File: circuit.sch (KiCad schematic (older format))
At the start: 35 parts, among them J1 CONN_8, J2 PASS_LED, J3 FAIL_LED, P1 PASS/FAIL, P2 RESET, Q1 FET-2N7000, Q2 FET-2N7000, Q3 FET-2N7000, U1 OpAmp-TLV2374, U2 Comp-LM339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

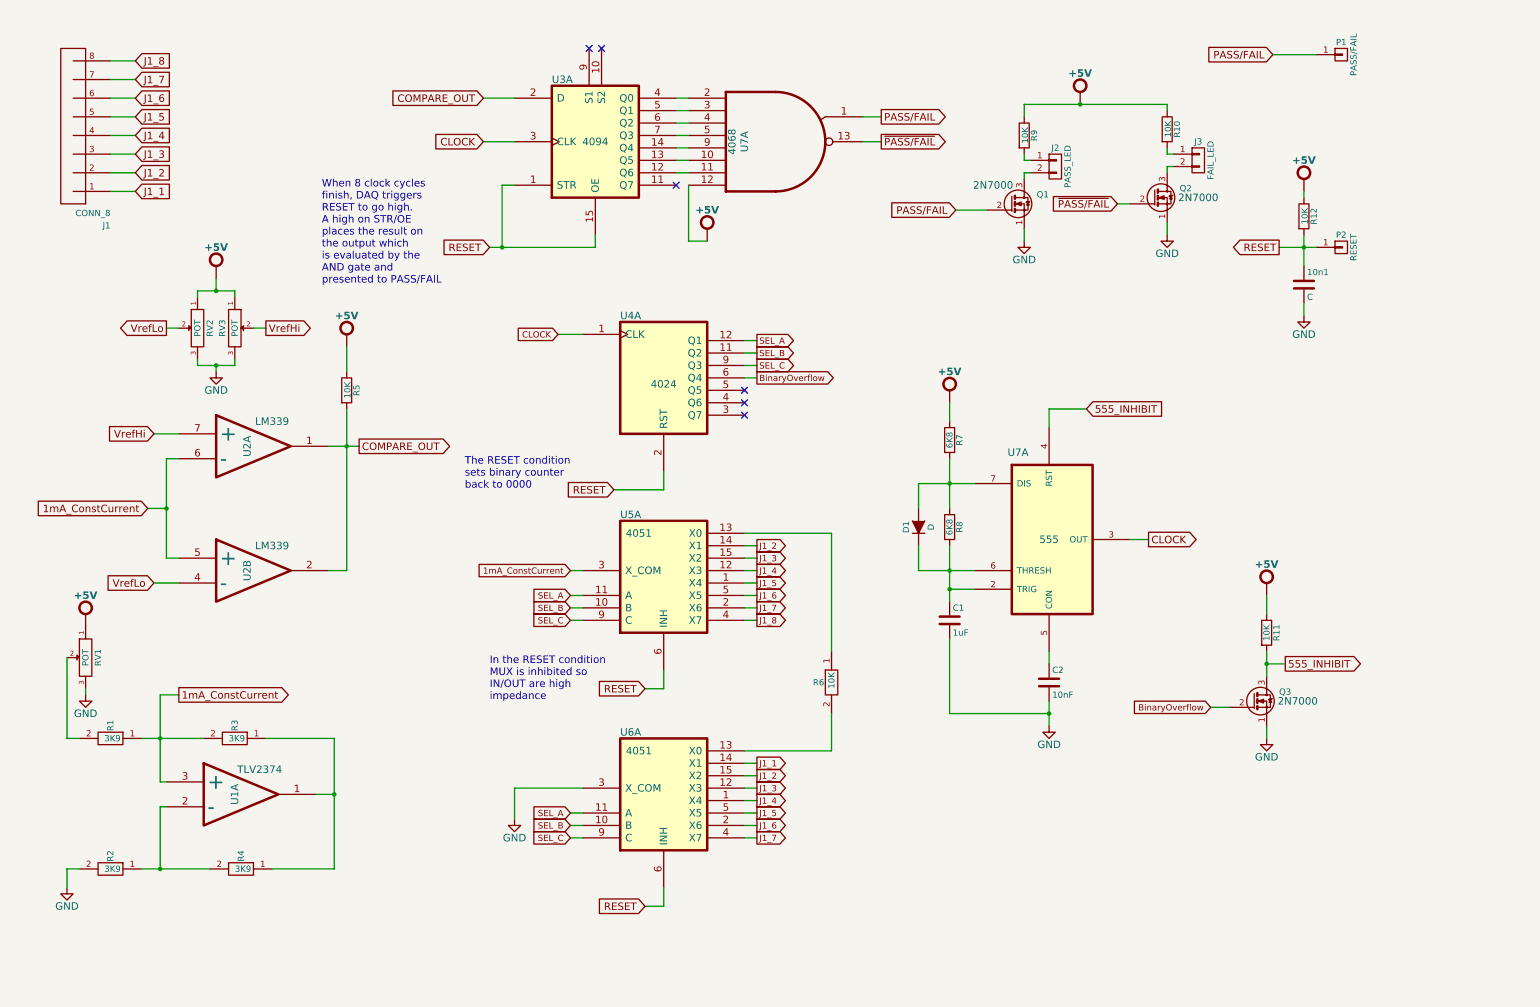
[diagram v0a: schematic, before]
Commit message: Added battery low detector and stripboard design (VeeCad)
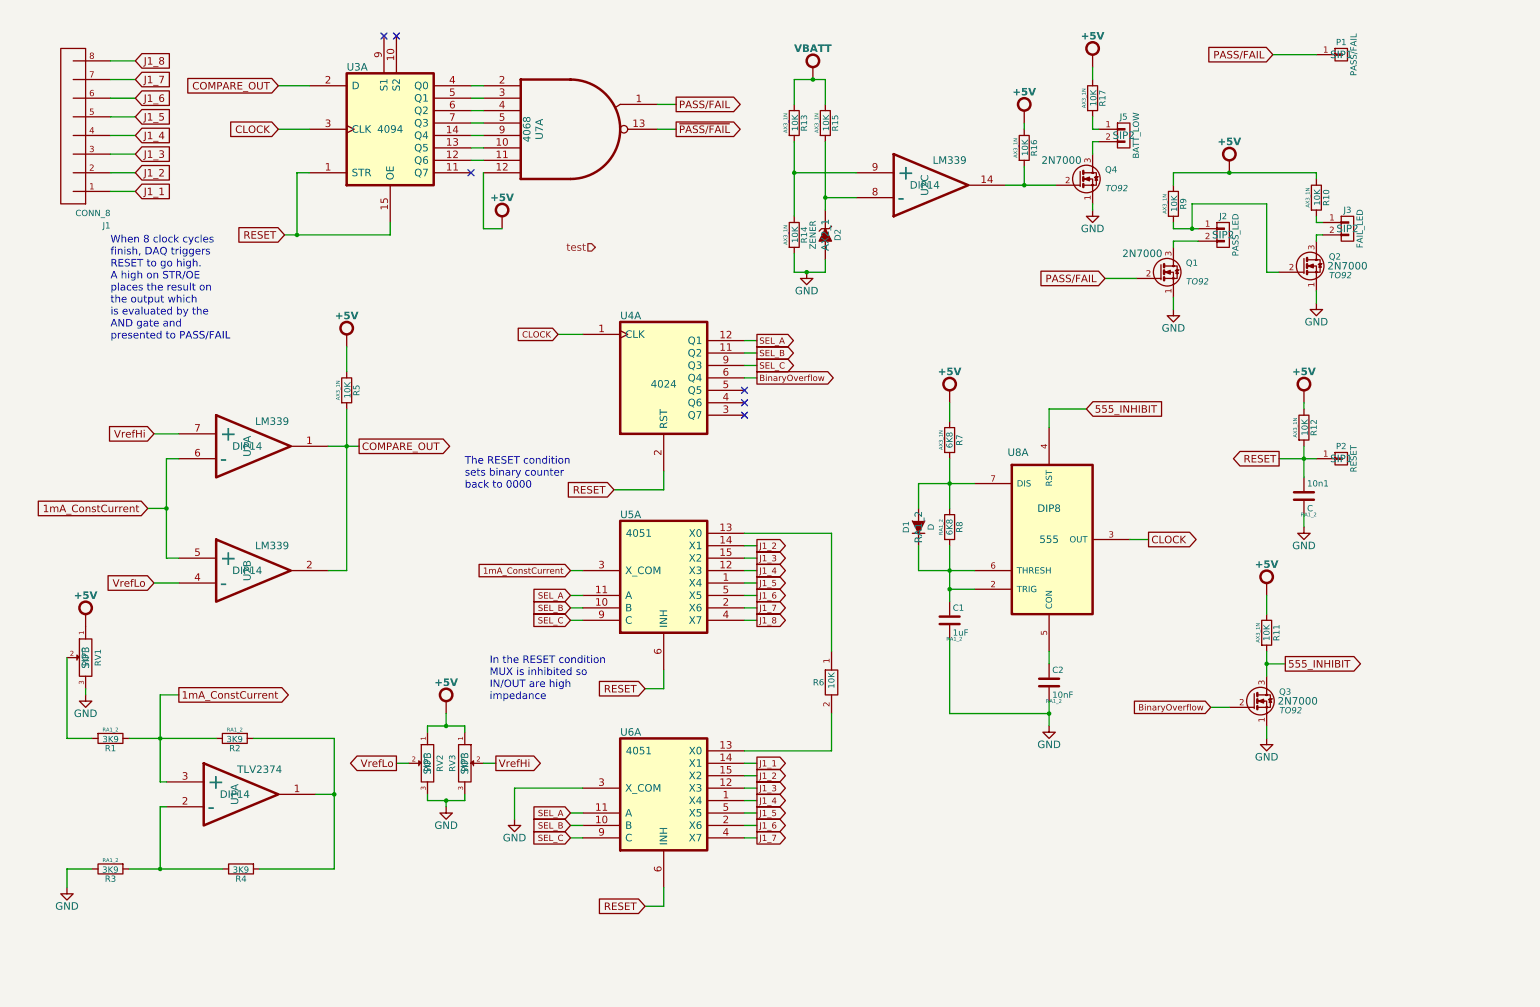
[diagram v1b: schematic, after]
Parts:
- removed R1, R2, R3, R4: 3K9, AX3_1N, symbol RESISTOR_0.25
- added D2: ZENER, AX2_1, symbol ZENER
- added J5: BATT_LOW, SIP2, symbol CONN_01X02
- added Q4: FET-2N7000, TO92, symbol FET-2N7000
- added R1, R2, R3, R4: 3K9, RA1_2, symbol R
- added R13, R14, R15, R16, R17: 10K, AX3_1N, symbol R
- added unit 3 of U2
- 10n1, C1, C2, D1, R8: footprint (none) -> RA1_2
- J2, J3: footprint (none) -> SIP2
- P1, P2: footprint (none) -> SIP1
- Q1, Q2, Q3: footprint (none) -> TO92
- R10, R11, R12, R5, R7, R9: footprint (none) -> AX3_1N
- RV1, RV2, RV3: footprint (none) -> SIP3
- U1, U2: footprint (none) -> DIP14
- U8: renamed from U7; footprint (none) -> DIP8
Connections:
- net +5V: now also R16.1, R17.1
- net 1mA_ConstCurrent: now also R1.1, R2.1
- net GND: now also D2.2 (A), Q4.1 (S), R14.2, R3.1
- net ~PASS/FAIL: no longer Q2.2 (G)
- net at U1.2 (-): now also R3.2, R4.1
- net at U1.1: now also R2.2, R4.2
- net at RV1.2: now also R1.2
- net at J2.1 (P1), R9.2: now also Q2.2 (G)
- new net: Q4.2 (G), R16.2, U2.14
- new net: D2.1 (K), R15.2, U2.8 (-)
- new net: R13.2, R14.1, U2.9 (+)
- new net: J5.2 (P2), Q4.3 (D)
- new net: J5.1 (P1), R17.2
- new net VBATT: R13.1, R15.1
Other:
- moved on the sheet: 10n1, J2, J3, P2, Q1, Q2, R10, R12, R9, RV2, RV3, U3A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

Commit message: Separated .net files for VeeCAD and KiCAD.  Associated footprints for KiCAD and started board layout
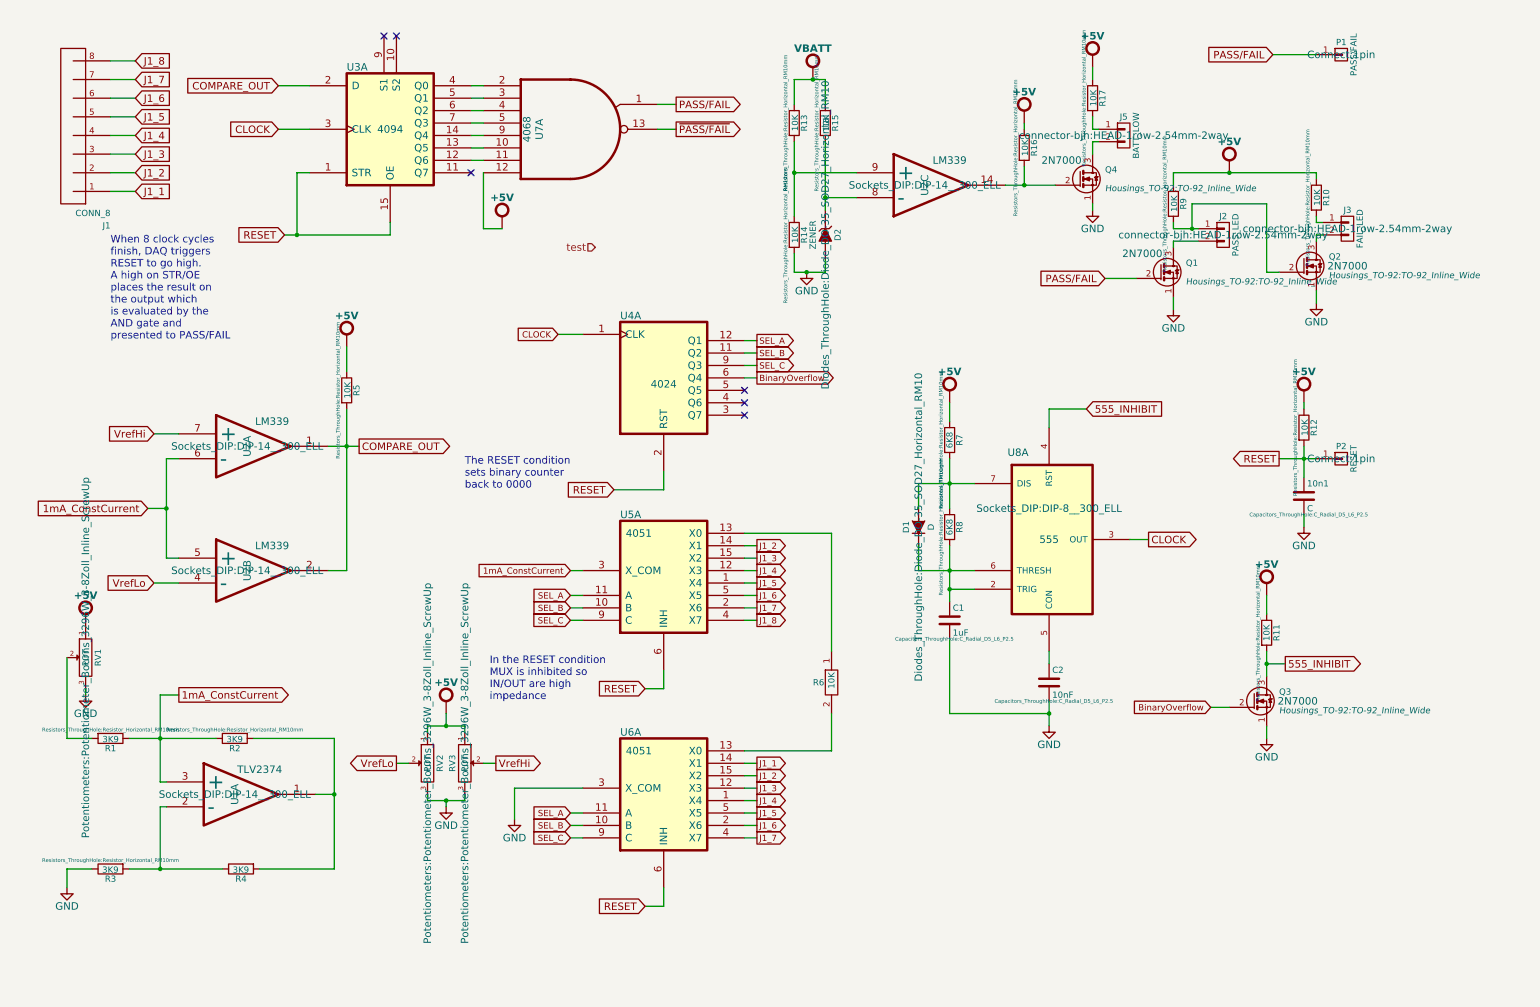
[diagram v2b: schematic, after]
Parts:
- 10n1, C1, C2: footprint RA1_2 -> Capacitors_ThroughHole:C_Radial_D5_L6_P2.5
- D1: footprint RA1_2 -> Diodes_ThroughHole:Diode_DO-35_SOD27_Horizontal_RM10
- D2: footprint AX2_1 -> Diodes_ThroughHole:Diode_DO-35_SOD27_Horizontal_RM10
- J1: footprint SIP8 -> connector-bjh:HEAD-1row-2.54mm-8way
- J2, J3, J5: footprint SIP2 -> connector-bjh:HEAD-1row-2.54mm-2way
- P1, P2: footprint SIP1 -> Connect:1pin
- Q1, Q2, Q3, Q4: footprint TO92 -> Housings_TO-92:TO-92_Inline_Wide
- R1, R2, R3, R4, R8: footprint RA1_2 -> Resistors_ThroughHole:Resistor_Horizontal_RM10mm
- R10, R11, R12, R13, R14, R15, R16, R17, R5, R6, R7, R9: footprint AX3_1N -> Resistors_ThroughHole:Resistor_Horizontal_RM10mm
- RV1, RV2, RV3: footprint SIP3 -> Potentiometers:Potentiometer_Bourns_3296W_3-8Zoll_Inline_ScrewUp
- U1, U2, U4, U7: footprint DIP14 -> Sockets_DIP:DIP-14__300_ELL
- U3, U5, U6: footprint DIP16 -> Sockets_DIP:DIP-16__300_ELL
- U8: footprint DIP8 -> Sockets_DIP:DIP-8__300_ELL
